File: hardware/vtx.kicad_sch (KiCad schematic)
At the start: 57 parts, among them J1 U.FL, Q27 BC857BM, Q28 AP1606, U19 RTC6705, U20 SE5004L, U21 LP5912-3.3, U22 LP5907-2.85, X4 8MHz 10pF

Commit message: Preserve owner schematic and board before final design review
Snapshot of the saved working design supplied for review.
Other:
- moved on the sheet: C135, C136, R89, R90

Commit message: Correct Whoop schematic and prepare component library for routing
Add local BMI270 bypassing, improve regulator capacitance margin, isolate
bidirectional DShot supply domains, and correct PA reference accuracy.
Remove Q28/R11 with matching firmware polarity and retain the proven
OpenFC-Lite OSD topology. Correct the receiver LED bypass rail.

Synchronize PCB connectivity, verify component pins and land patterns,
and provide firmware bindings plus placement/layer guidance. Replace stale
manual BOM and interface plans with schematic-derived exports.

Validation: ERC 0, seven netlist checks, 48 footprint checks, 22 rule
behavior cases, and PCB schematic parity 0. The parked PCB retains layout
DRC findings and 499 unconnected items; no manufacturing or flight release.
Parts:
- removed Q28: AP1606, lib:DFN-3L_L1.0-W0.6-P0.65-BR_W, symbol lib:AP1606
- U22: value LP5907-2.85 -> TPS7A20285; symbol lib:LP5907SNX-2.85 -> lib:TPS7A20285PDQN; LCSC C2872477 -> C3748388; MPN LP5907SNX-2.85/NOPB -> TPS7A20285PDQNR
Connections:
- net VTX_PWR_EN is gone; now on net HD_EN: R68.2, U21.4 (EN)
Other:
- note added: "PA REFERENCE TPS7A20-2.85"
- note removed: "PA REFERENCE LP5907-2.85"
- moved on the sheet: C135, C136, R89, R90

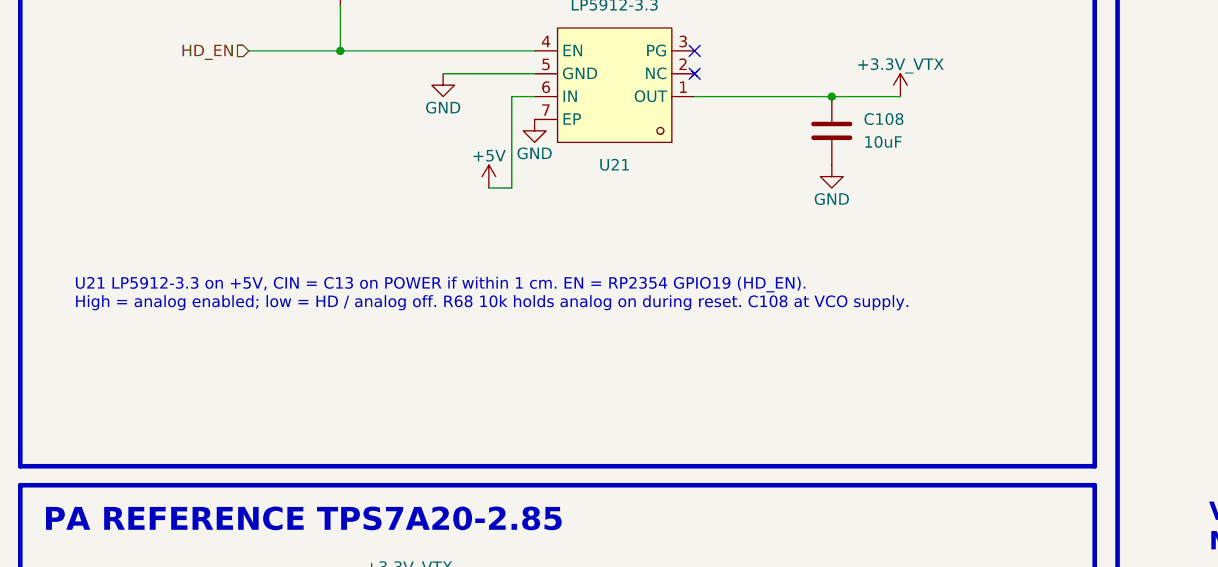
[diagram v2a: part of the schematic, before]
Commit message: Route flash receiver controls and power entry with scoped reference checks
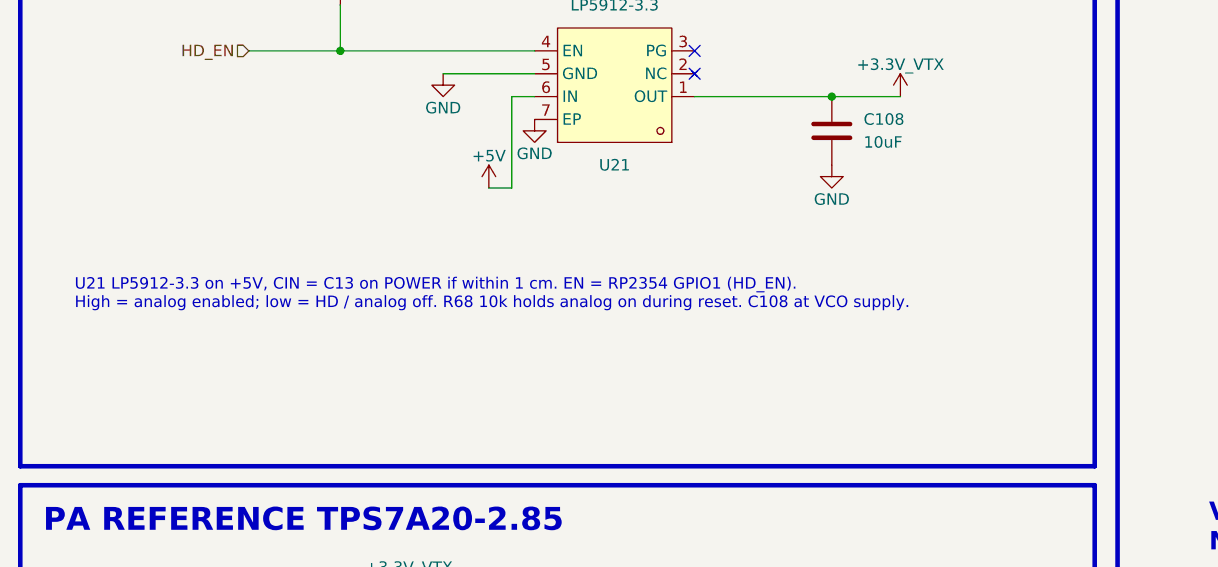
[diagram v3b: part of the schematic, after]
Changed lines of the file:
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@@
 		)
 	)
-	(text_box "U21 LP5912-3.3 on +5V, CIN = C13 on POWER if within 1 cm. EN = RP2354 GPIO19 (HD_EN).\nHigh = analog enabled; low = HD / analog off. R68 10k holds analog on during reset. C108 at VCO supply."
+	(text_box "U21 LP5912-3.3 on +5V, CIN = C13 on POWER if within 1 cm. EN = RP2354 GPIO1 (HD_EN).\nHigh = analog enabled; low = HD / analog off. R68 10k holds analog on during reset. C108 at VCO supply."
 		(exclude_from_sim no)
 		(at 20.32 86.36 0)
